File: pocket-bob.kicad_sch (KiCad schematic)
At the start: 131 parts, among them J3 Conn_01x18, J4 Conn_01x18, J5 Conn_01x18, J6 Conn_01x18, J7 USB_A, P1 Conn_02x18_Odd_Even, P2 Conn_02x18_Odd_Even, U1 TPD3S014

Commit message: Some finishing touches
Remove VIN_USB LED.
Give resistors and LEDs some values.
Update the pours.
Update the silkscreen with board revision.
Update all plots.

Signed-off-by: Michael Welling <mwelling79@gmail.com>
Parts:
- removed D4: LED, LED_SMD:LED_0402_1005Metric, symbol Device:LED
- removed R4: R, Resistor_SMD:R_0402_1005Metric, symbol Device:R
- D1, D25, D30, D43, D45, D48: value LED -> RED
- D10, D11, D12, D13, D14, D15, D16, D17, D18, D19, D20, D21, D22, D23, D24, D27, D28, D31, D32, D33, D34, D35, D36, D37, D38, D39, D40, D41, D42, D46, D49, D50, D51, D52, D53, D54, D55, D56, D57, D58, D59, D63, D64, D65, D66, D68, D69, D70, D71, D72: value LED -> GREEN
- R1: value R -> 2.2K
- R10, R11, R12, R13, R14, R15, R16, R17, R18, R19, R20, R21, R22, R23, R24, R25, R27, R28, R30, R31, R32, R33, R34, R35, R36, R37, R38, R39, R40, R41, R42, R43, R45, R46, R48, R49, R50, R51, R52, R53, R54, R55, R56, R57, R58, R59, R63, R64, R65, R66, R68, R69, R70, R71, R72: value R -> 1K

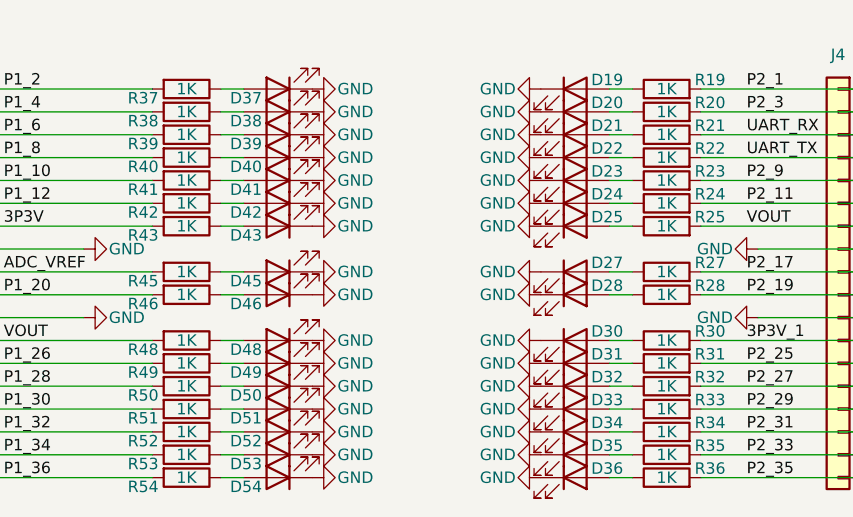
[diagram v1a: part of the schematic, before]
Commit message: Small updates
Switched all 5V LED current limiting resistors to 2.2K.
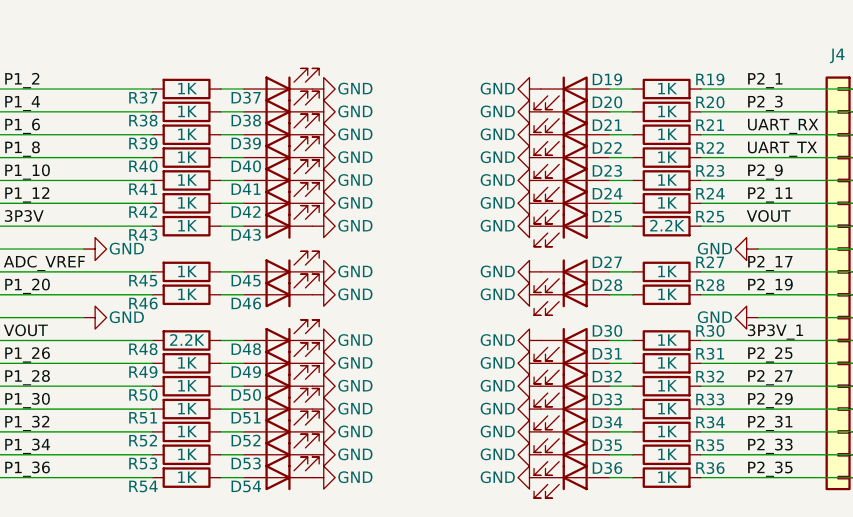
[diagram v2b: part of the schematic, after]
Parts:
- R25, R48: value 1K -> 2.2K
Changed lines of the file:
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@@
 			)
 		)
-		(property "Value" "1K"
+		(property "Value" "2.2K"
 			(at 179.07 90.17 90)
 			(effects
@@
 			)
 		)
-		(property "Value" "1K"
+		(property "Value" "2.2K"
 			(at 125.73 102.87 90)
 			(effects

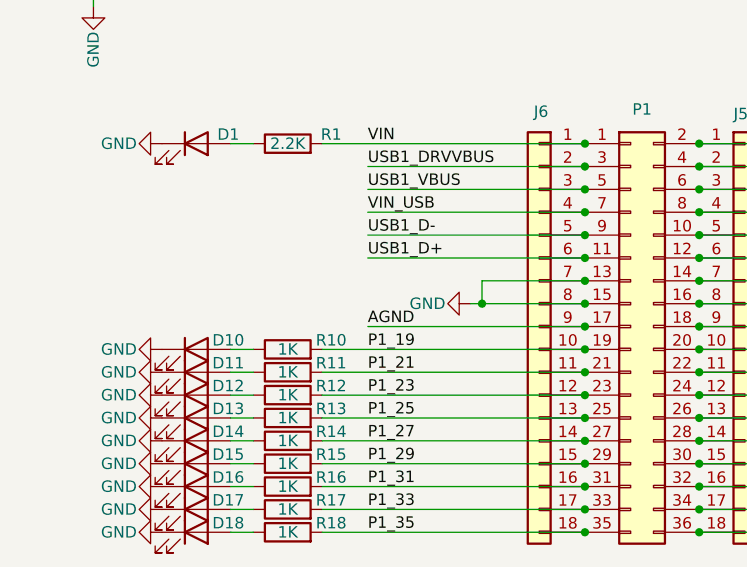
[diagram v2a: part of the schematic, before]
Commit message: Switch P1_13 to LED instead of GND
The USB_ID functionality is not need if we aren't using OTG.

Signed-off-by: Michael Welling <mwelling79@gmail.com>
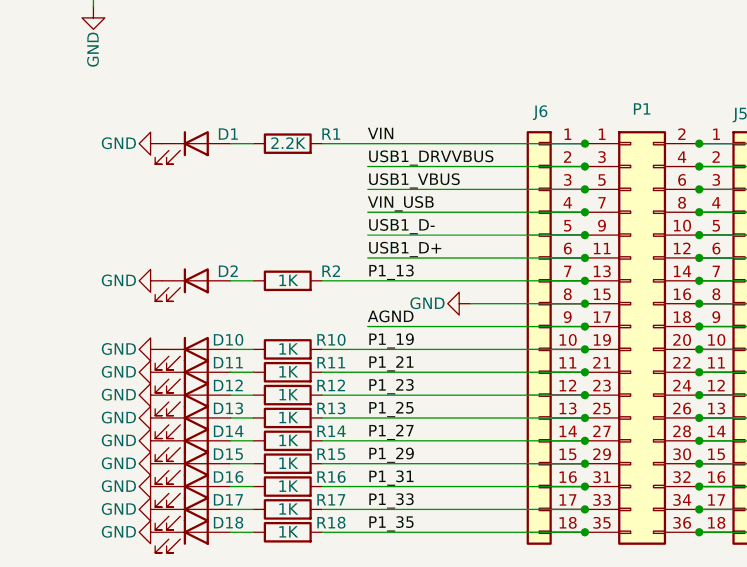
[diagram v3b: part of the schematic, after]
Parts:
- added D2: GREEN, LED_SMD:LED_0402_1005Metric, symbol Device:LED
- added R2: 1K, Resistor_SMD:R_0402_1005Metric, symbol Device:R
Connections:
- net GND: now also D2.1 (K); no longer J6.7 (Pin_7), P1.13 (Pin_13)
- new net: D2.2 (A), R2.1
- new net P1_13: J6.7 (Pin_7), P1.13 (Pin_13), R2.2
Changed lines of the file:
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@@
 	)
 	(junction
+		(at 83.82 90.17)
+		(diameter 0)
+		(color 0 0 0 0)
+	)
+	(junction
 		(at 96.52 107.95)
 		(diameter 0)
@@
 	)
 	(junction
-		(at 72.39 92.71)
-		(diameter 0)
-		(color 0 0 0 0)
-	)
-	(junction
 		(at 83.82 92.71)
 		(diameter 0)
@@
 	)
 	(junction
-		(at 83.82 90.17)
-		(diameter 0)
-		(color 0 0 0 0)
-	)
-	(junction
 		(at 215.9 95.25)
 		(diameter 0)
@@
 	(wire
 		(pts
-			(xy 236.22 110.49) (xy 215.9 110.49)
+			(xy 44.45 90.17) (xy 46.99 90.17)
 		)
 		(stroke
@@
 	(wire
 		(pts
-			(xy 236.22 113.03) (xy 215.9 113.03)
+			(xy 236.22 110.49) (xy 215.9 110.49)
 		)
 		(stroke
@@
 	(wire
 		(pts
-			(xy 91.44 43.18) (xy 77.47 43.18)
+			(xy 236.22 113.03) (xy 215.9 113.03)
 		)
 		(stroke
@@
 	(wire
 		(pts
-			(xy 236.22 97.79) (xy 215.9 97.79)
+			(xy 91.44 43.18) (xy 77.47 43.18)
 		)
 		(stroke
@@
 	(wire
 		(pts
-			(xy 182.88 74.93) (xy 203.2 74.93)
+			(xy 236.22 97.79) (xy 215.9 97.79)
 		)
 		(stroke
@@
 	(wire
 		(pts
-			(xy 44.45 118.11) (xy 46.99 118.11)
+			(xy 182.88 74.93) (xy 203.2 74.93)
 		)
 		(stroke
@@
 	(wire
 		(pts
-			(xy 72.39 90.17) (xy 83.82 90.17)
+			(xy 44.45 118.11) (xy 46.99 118.11)
 		)
 		(stroke
@@
 	(wire
 		(pts
-			(xy 71.12 92.71) (xy 72.39 92.71)
-		)
-		(stroke
-			(width 0)
-			(type default)
-		)
-	)
-	(wire
-		(pts
 			(xy 44.45 100.33) (xy 46.99 100.33)
 		)
@@
 	(wire
 		(pts
-			(xy 72.39 92.71) (xy 83.82 92.71)
+			(xy 71.12 92.71) (xy 83.82 92.71)
 		)
 		(stroke
@@
 	(wire
 		(pts
-			(xy 72.39 90.17) (xy 72.39 92.71)
-		)
-		(stroke
-			(width 0)
-			(type default)
-		)
-	)
-	(wire
-		(pts
 			(xy 236.22 90.17) (xy 215.9 90.17)
 		)
@@
 	(wire
 		(pts
+			(xy 54.61 90.17) (xy 83.82 90.17)
+		)
+		(stroke
+			(width 0)
+			(type default)
+		)
+	)
+	(wire
+		(pts
 			(xy 132.08 105.41) (xy 129.54 105.41)
 		)
@@
 		)
 	)
+	(label "P1_13"
+		(at 59.69 90.17 0)
+		(effects
+			(font
+				(size 1.27 1.27)
+			)
+			(justify left bottom)
+		)
+	)
 	(label "P2_24"
 		(at 224.79 102.87 0)
@@
 	)
 	(symbol
+		(lib_id "Device:LED")
+		(at 40.64 90.17 0)
+		(unit 1)
+		(exclude_from_sim no)
+		(in_bom yes)
+		(on_board yes)
+		(dnp no)
+		(property "Reference" "D2"
+			(at 44.196 89.154 0)
+			(effects
+				(font
+					(size 1.27 1.27)
+				)
+			)
+		)
+		(property "Value" "GREEN"
+			(at 37.338 89.154 0)
+			(effects
+				(font
+					(size 1.27 1.27)
+				)
+				(hide yes)
+			)
+		)
+		(property "Footprint" "LED_SMD:LED_0402_1005Metric"
+			(at 40.64 90.17 0)
+			(effects
+				(font
+					(size 1.27 1.27)
+				)
+				(hide yes)
+			)
+		)
+		(property "Datasheet" "~"
+			(at 40.64 90.17 0)
+			(effects
+				(font
+					(size 1.27 1.27)
+				)
+				(hide yes)
+			)
+		)
+		(property "Description" "Light emitting diode"
+			(at 40.64 90.17 0)
+			(effects
+				(font
+					(size 1.27 1.27)
+				)
+				(hide yes)
+			)
+		)
+		(pin "2"
+		)
+		(pin "1"
+		)
+		(instances
+			(project "pocket-bob"
+				(path "/80a48dc9-34e5-4985-ad01-29d7823c9fb7"
+					(reference "D2")
+					(unit 1)
+				)
+			)
+		)
+	)
+	(symbol
 		(lib_id "power:GND")
 		(at 254 74.93 90)
@@
 	)
 	(symbol
+		(lib_id "power:GND")
+		(at 36.83 90.17 270)
+		(unit 1)
+		(exclude_from_sim no)
+		(in_bom yes)
+		(on_board yes)
+		(dnp no)
+		(property "Reference" "#PWR060"
+			(at 30.48 90.17 0)
+			(effects
+				(font
+					(size 1.27 1.27)
+				)
+				(hide yes)
+			)
+		)
+		(property "Value" "GND"
+			(at 34.036 90.17 90)
+			(effects
+				(font
+					(size 1.27 1.27)
+				)
+				(justify right)
+			)
+		)
+		(property "Footprint" ""
+			(at 36.83 90.17 0)
+			(effects
+				(font
+					(size 1.27 1.27)
+				)
+				(hide yes)
+			)
+		)
+		(property "Datasheet" ""
+			(at 36.83 90.17 0)
+			(effects
+				(font
+					(size 1.27 1.27)
+				)
+				(hide yes)
+			)
+		)
+		(property "Description" "Power symbol creates a global label with name \"GND\" , ground"
+			(at 36.83 90.17 0)
+			(effects
+				(font
+					(size 1.27 1.27)
+				)
+				(hide yes)
+			)
+		)
+		(pin "1"
+		)
+		(instances
+			(project "pocket-bob"
+				(path "/80a48dc9-34e5-4985-ad01-29d7823c9fb7"
+					(reference "#PWR060")
+					(unit 1)
+				)
+			)
+		)
+	)
+	(symbol
 		(lib_id "Device:R")
 		(at 125.73 90.17 270)
@@
 					(unit 1)
 				)
+			)
+		)
+	)
+	(symbol
+		(lib_id "Device:R")
+		(at 50.8 90.17 90)
+		(unit 1)
+		(exclude_from_sim no)
+		(in_bom yes)
+		(on_board yes)
+		(dnp no)
+		(property "Reference" "R2"
+			(at 55.626 89.154 90)
+			(effects
+				(font
+					(size 1.27 1.27)
+				)
+			)
+		)
+		(property "Value" "1K"
+			(at 50.8 90.17 90)
+			(effects
+				(font
+					(size 1.27 1.27)
+				)
+			)
+		)
+		(property "Footprint" "Resistor_SMD:R_0402_1005Metric"
+			(at 50.8 91.948 90)
+			(effects
+				(font
+					(size 1.27 1.27)
+				)
+				(hide yes)
+			)
+		)
+		(property "Datasheet" "~"
+			(at 50.8 90.17 0)
+			(effects
+				(font
+					(size 1.27 1.27)
+				)
+				(hide yes)
+			)
+		)
+		(property "Description" "Resistor"
+			(at 50.8 90.17 0)
+			(effects
+				(font
+					(size 1.27 1.27)
+				)
+				(hide yes)
+			)
+		)
+		(pin "2"
+		)
+		(pin "1"
+		)
+		(instances
+			(project "pocket-bob"
+				(path "/80a48dc9-34e5-4985-ad01-29d7823c9fb7"
+					(reference "R2")
+					(unit 1)
+				)

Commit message: Add digikey part number for components
Signed-off-by: Michael Welling <mwelling79@gmail.com>
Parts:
- C1: VPN (none) -> 311-1088-1-ND
- C2: VPN (none) -> 399-C0603X154K4RACTUCT-ND
- D1, D25, D30, D43, D45, D48: VPN (none) -> 1516-1217-1-ND
- D10, D11, D12, D13, D14, D15, D16, D17, D18, D19, D2, D20, D21, D22, D23, D24, D27, D28, D31, D32, D33, D34, D35, D36, D37, D38, D39, D40, D41, D42, D46, D49, D50, D51, D52, D53, D54, D55, D56, D57, D58, D59, D63, D64, D65, D66, D68, D69, D70, D71, D72: VPN (none) -> 1516-1216-1-ND
- FB1, FB2: VPN (none) -> 240-2367-1-ND
- J3, J4, J5, J6, P1, P2: VPN (none) -> WM50012-36-ND
- J7: VPN (none) -> WM14667-ND
- R1, R25, R48: VPN (none) -> P2.20KLCT-ND
- R10, R11, R12, R13, R14, R15, R16, R17, R18, R19, R2, R20, R21, R22, R23, R24, R27, R28, R30, R31, R32, R33, R34, R35, R36, R37, R38, R39, R40, R41, R42, R43, R45, R46, R49, R50, R51, R52, R53, R54, R55, R56, R57, R58, R59, R63, R64, R65, R66, R68, R69, R70, R71, R72: VPN (none) -> P1.00KLCT-ND
- R3: VPN (none) -> 311-4.7KJRCT-ND
- U1: VPN (none) -> 296-38835-1-ND
